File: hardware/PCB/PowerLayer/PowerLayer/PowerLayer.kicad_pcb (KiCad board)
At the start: 2 copper layers, 81.5 x 58.2 mm, 2 parts, among them J1 Conn_01x03_Female

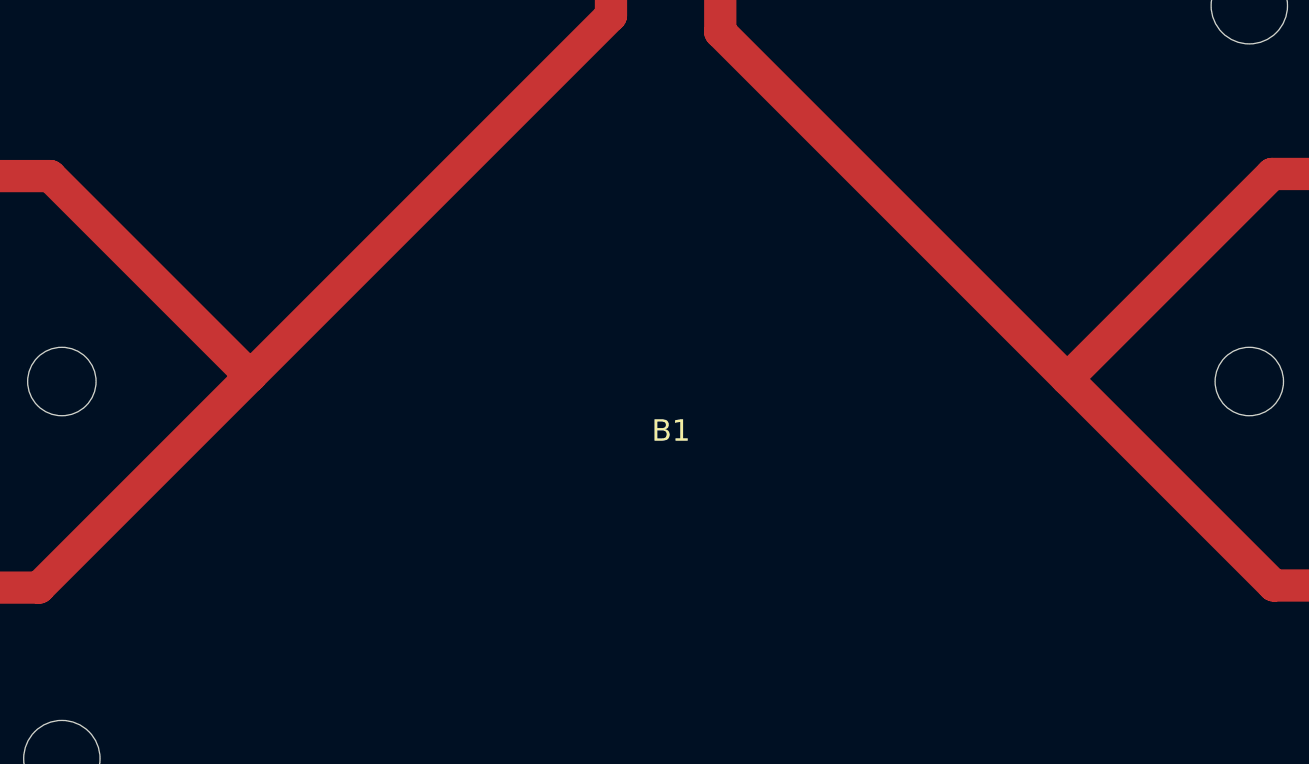
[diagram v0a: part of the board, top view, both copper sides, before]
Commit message: PowerLayer PCB batterys polarization label added
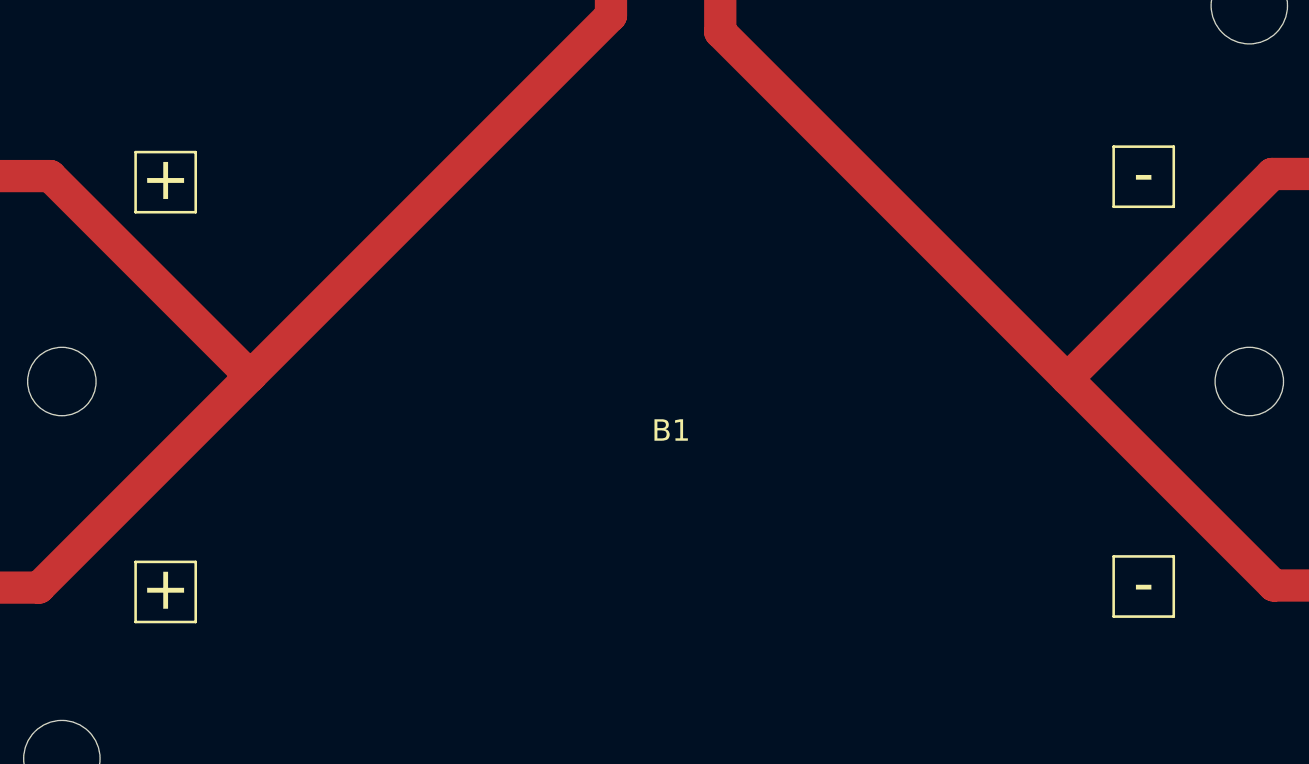
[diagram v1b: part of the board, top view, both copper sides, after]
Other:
- board text added: "+"
- board text added: "-"
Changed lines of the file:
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@@
   (general
     (thickness 1.6)
-    (drawings 14)
+    (drawings 34)
     (tracks 13)
     (zones 0)
@@
   )
   (setup
-    (last_trace_width 1.5)
+    (last_trace_width 0.25)
     (user_trace_width 1.5)
     (trace_clearance 0.2)
@@
       (effects (font (size 1 1) (thickness 0.15)))
     )
+    (fp_line (start -1.27 -1.27) (end 0.635 -1.27) (layer F.Fab) (width 0.1))
+    (fp_line (start 0.635 -1.27) (end 1.27 -0.635) (layer F.Fab) (width 0.1))
+    (fp_line (start 1.27 -0.635) (end 1.27 6.35) (layer F.Fab) (width 0.1))
+    (fp_line (start 1.27 6.35) (end -1.27 6.35) (layer F.Fab) (width 0.1))
+    (fp_line (start -1.27 6.35) (end -1.27 -1.27) (layer F.Fab) (width 0.1))
+    (fp_line (start -1.33 1.27) (end 1.33 1.27) (layer F.SilkS) (width 0.12))
+    (fp_line (start -1.33 1.27) (end -1.33 6.41) (layer F.SilkS) (width 0.12))
+    (fp_line (start -1.33 6.41) (end 1.33 6.41) (layer F.SilkS) (width 0.12))
+    (fp_line (start 1.33 1.27) (end 1.33 6.41) (layer F.SilkS) (width 0.12))
+    (fp_line (start 1.33 -1.33) (end 1.33 0) (layer F.SilkS) (width 0.12))
+    (fp_line (start 0 -1.33) (end 1.33 -1.33) (layer F.SilkS) (width 0.12))
+    (fp_line (start -1.8 -1.8) (end 1.75 -1.8) (layer F.CrtYd) (width 0.05))
+    (fp_line (start 1.75 -1.8) (end 1.75 6.85) (layer F.CrtYd) (width 0.05))
+    (fp_line (start 1.75 6.85) (end -1.8 6.85) (layer F.CrtYd) (width 0.05))
     (fp_line (start -1.8 6.85) (end -1.8 -1.8) (layer F.CrtYd) (width 0.05))
-    (fp_line (start 1.75 6.85) (end -1.8 6.85) (layer F.CrtYd) (width 0.05))
-    (fp_line (start 1.75 -1.8) (end 1.75 6.85) (layer F.CrtYd) (width 0.05))
-    (fp_line (start -1.8 -1.8) (end 1.75 -1.8) (layer F.CrtYd) (width 0.05))
-    (fp_line (start 0 -1.33) (end 1.33 -1.33) (layer F.SilkS) (width 0.12))
-    (fp_line (start 1.33 -1.33) (end 1.33 0) (layer F.SilkS) (width 0.12))
-    (fp_line (start 1.33 1.27) (end 1.33 6.41) (layer F.SilkS) (width 0.12))
-    (fp_line (start -1.33 6.41) (end 1.33 6.41) (layer F.SilkS) (width 0.12))
-    (fp_line (start -1.33 1.27) (end -1.33 6.41) (layer F.SilkS) (width 0.12))
-    (fp_line (start -1.33 1.27) (end 1.33 1.27) (layer F.SilkS) (width 0.12))
-    (fp_line (start -1.27 6.35) (end -1.27 -1.27) (layer F.Fab) (width 0.1))
-    (fp_line (start 1.27 6.35) (end -1.27 6.35) (layer F.Fab) (width 0.1))
-    (fp_line (start 1.27 -0.635) (end 1.27 6.35) (layer F.Fab) (width 0.1))
-    (fp_line (start 0.635 -1.27) (end 1.27 -0.635) (layer F.Fab) (width 0.1))
-    (fp_line (start -1.27 -1.27) (end 0.635 -1.27) (layer F.Fab) (width 0.1))
     (fp_text user %R (at 0 2.54) (layer F.Fab)
       (effects (font (size 1 1) (thickness 0.15)))
@@
       (effects (font (size 1 1) (thickness 0.15)))
     )
+    (fp_line (start -4 -39) (end 76 -39) (layer F.SilkS) (width 0.12))
+    (fp_line (start 76 4) (end 76 -39) (layer F.SilkS) (width 0.12))
+    (fp_line (start -4 4) (end -4 -39) (layer F.SilkS) (width 0.12))
     (fp_line (start -4 4) (end 76 4) (layer F.SilkS) (width 0.12))
-    (fp_line (start -4 4) (end -4 -39) (layer F.SilkS) (width 0.12))
-    (fp_line (start 76 4) (end 76 -39) (layer F.SilkS) (width 0.12))
-    (fp_line (start -4 -39) (end 76 -39) (layer F.SilkS) (width 0.12))
     (pad "" np_thru_hole circle (at 72.22 0) (size 2.38 2.38) (drill 2.38) (layers *.Cu *.Mask))
     (pad "" np_thru_hole circle (at 63.71 -35) (size 3.55 3.55) (drill 3.55) (layers *.Cu *.Mask))
@@
     )
   )
+  (gr_text + (at 82.422217 131.300546) (layer F.SilkS)
+    (effects (font (size 2 2) (thickness 0.15)))
+  )
+  (gr_text + (at 82.422217 150.350546) (layer F.SilkS)
+    (effects (font (size 2 2) (thickness 0.15)))
+  )
+  (gr_line (start 83.82 149.098) (end 83.82 151.892) (layer F.SilkS) (width 0.12))
+  (gr_line (start 83.82 151.892) (end 81.026 151.892) (layer F.SilkS) (width 0.12))
+  (gr_line (start 81.026 151.892) (end 81.026 149.098) (layer F.SilkS) (width 0.12))
+  (gr_line (start 83.82 132.842) (end 81.026 132.842) (layer F.SilkS) (width 0.12))
+  (gr_line (start 81.026 149.098) (end 83.82 149.098) (layer F.SilkS) (width 0.12))
+  (gr_line (start 81.026 132.842) (end 81.026 130.048) (layer F.SilkS) (width 0.12))
+  (gr_line (start 81.026 130.048) (end 83.82 130.048) (layer F.SilkS) (width 0.12))
+  (gr_line (start 83.82 130.048) (end 83.82 132.842) (layer F.SilkS) (width 0.12))
+  (gr_text - (at 127.888217 150.096546) (layer F.SilkS)
+    (effects (font (size 2 2) (thickness 0.15)))
+  )
+  (gr_line (start 129.286 151.638) (end 126.492 151.638) (layer F.SilkS) (width 0.12))
+  (gr_line (start 126.492 151.638) (end 126.492 148.844) (layer F.SilkS) (width 0.12))
+  (gr_line (start 126.492 148.844) (end 129.286 148.844) (layer F.SilkS) (width 0.12))
+  (gr_line (start 129.286 148.844) (end 129.286 151.638) (layer F.SilkS) (width 0.12))
+  (gr_line (start 126.492 132.588) (end 126.492 129.794) (layer F.SilkS) (width 0.12))
+  (gr_line (start 129.286 132.588) (end 126.492 132.588) (layer F.SilkS) (width 0.12))
+  (gr_line (start 129.286 129.794) (end 129.286 132.588) (layer F.SilkS) (width 0.12))
+  (gr_line (start 126.492 129.794) (end 129.286 129.794) (layer F.SilkS) (width 0.12))
+  (gr_text - (at 127.888217 131.046546) (layer F.SilkS)
+    (effects (font (size 2 2) (thickness 0.15)))
+  )
   (dimension 81.534 (width 0.15) (layer Dwgs.User)

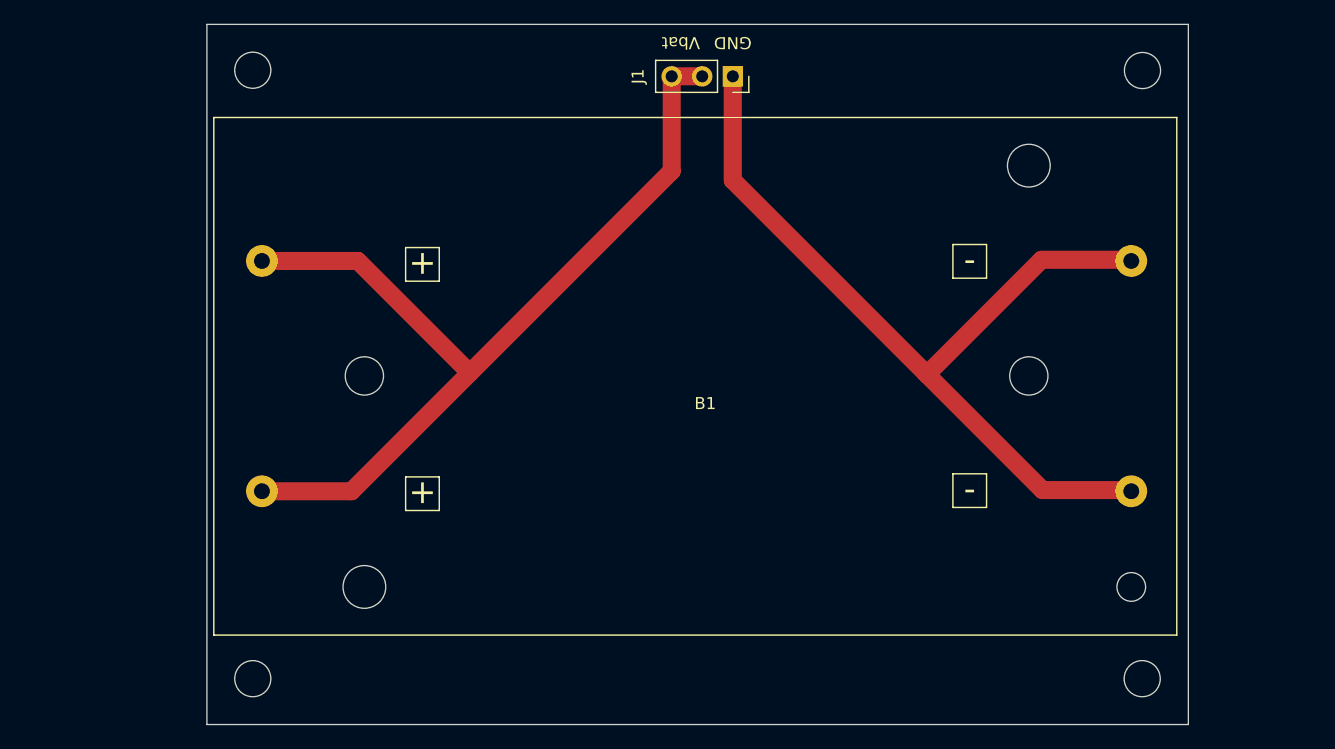
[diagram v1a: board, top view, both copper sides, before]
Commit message: Final casing selected and PCB rearranged to fit into the casing
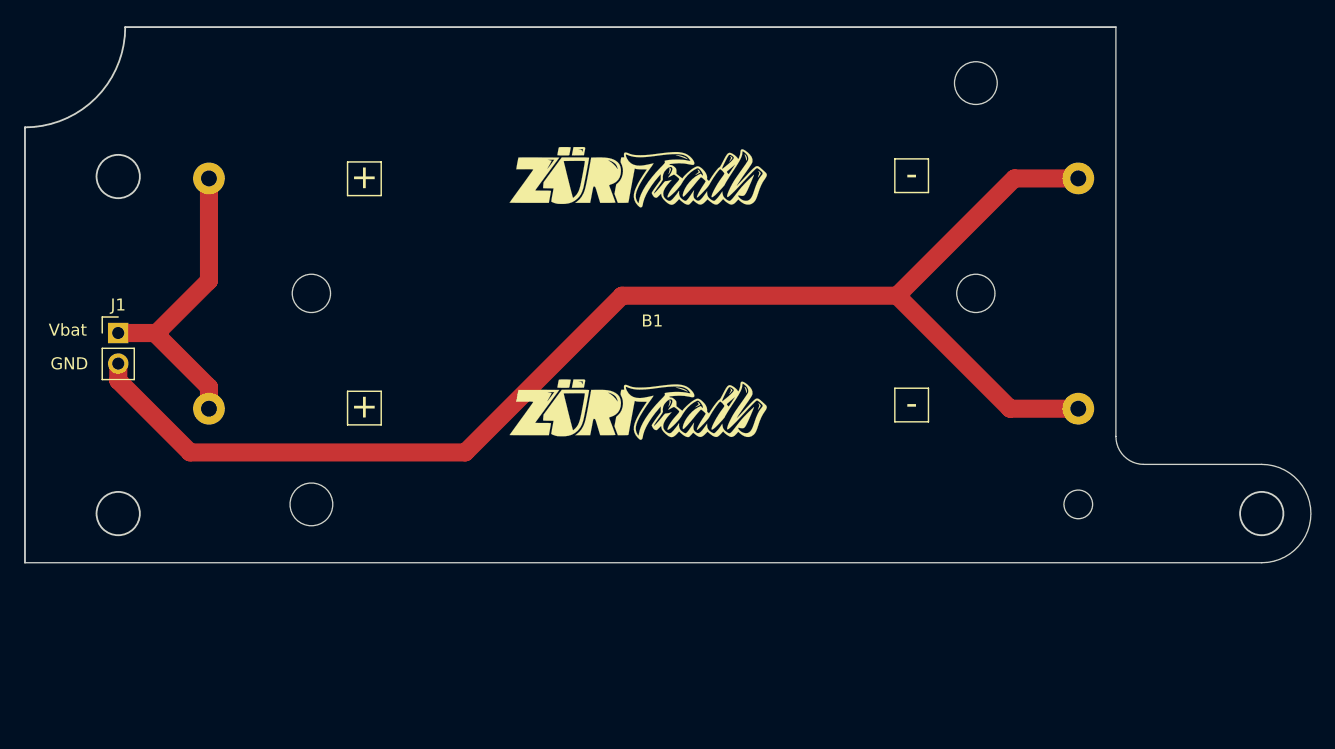
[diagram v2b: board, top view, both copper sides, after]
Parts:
- added G***: LOGO, GraphicsLib:ZueriTrailsLogo_small, F.Cu at (100.3, 124.2)
- added G***: LOGO, GraphicsLib:ZueriTrailsLogo_small, F.Cu at (100.3, 143.5)
- J1: value Conn_01x03_Female -> Logic layer connection; footprint Connector_PinSocket_2.54mm:PinSocket_1x03_P2.54mm_Vertical -> Connector_PinHeader_2.54mm:PinHeader_1x02_P2.54mm_Vertical
- moved J1 55.3 mm to (57.1, 137.1), turned to 0 degrees
- moved B1 8.15 mm to (64.7, 151.4)
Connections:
- J1 pad 1: GND -> +3V8
- J1 pad 2: +3V8 -> GND
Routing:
- net +3V8: track 76.6 -> 29.0 mm
- net GND: track 73.3 -> 112.0 mm
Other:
- board size 81.5 x 58.2 mm -> 106.8 x 44.5 mm

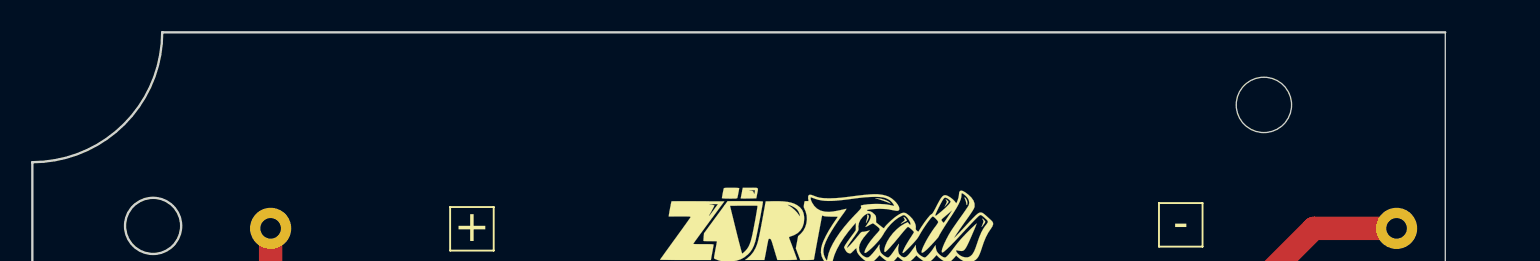
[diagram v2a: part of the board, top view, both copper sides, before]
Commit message: PCB adjusted and BOM started
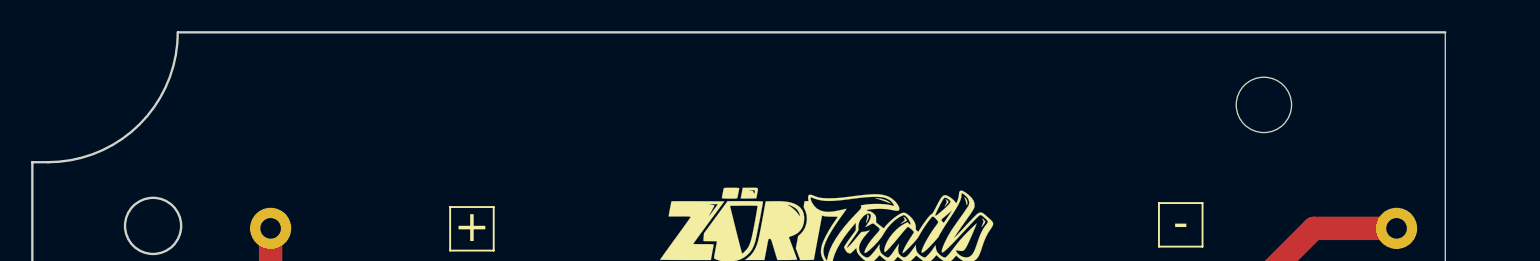
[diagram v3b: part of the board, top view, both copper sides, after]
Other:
- outline, holes or cut-outs redrawn

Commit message: BOM finished and Gerber files created
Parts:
- added REF**: MountingHole_3.5mm_Pad, MountingHole:MountingHole_3.5mm_Pad, F.Cu at (152.1, 152.1)
- added REF**: MountingHole_3.5mm_Pad, MountingHole:MountingHole_3.5mm_Pad, F.Cu at (57.1, 152.1)
- added REF**: MountingHole_3.5mm_Pad, MountingHole:MountingHole_3.5mm_Pad, F.Cu at (57.1, 124.1)
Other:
- outline, holes or cut-outs redrawn
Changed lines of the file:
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@@
   (general
     (thickness 1.6)
-    (drawings 43)
+    (drawings 39)
     (tracks 15)
     (zones 0)
-    (modules 4)
+    (modules 7)
     (nets 3)
   )
@@
     (pcbplotparams
       (layerselection 0x010fc_ffffffff)
-      (usegerberextensions false)
-      (usegerberattributes true)
-      (usegerberadvancedattributes true)
-      (creategerberjobfile true)
+      (usegerberextensions true)
+      (usegerberattributes false)
+      (usegerberadvancedattributes false)
+      (creategerberjobfile false)
       (excludeedgelayer true)
       (linewidth 0.100000)
@@
       (psa4output false)
       (plotreference true)
-      (plotvalue true)
+      (plotvalue false)
       (plotinvisibletext false)
       (padsonsilk false)
-      (subtractmaskfromsilk false)
+      (subtractmaskfromsilk true)
       (outputformat 1)
       (mirror false)
-      (drillshape 1)
+      (drillshape 0)
       (scaleselection 1)
-      (outputdirectory ""))
+      (outputdirectory "GerberFiles/v0.1/"))
   )
   (net 0 "")
@@
     (uvia_dia 0.3)
     (uvia_drill 0.1)
+  )
+  (module MountingHole:MountingHole_3.5mm_Pad (layer F.Cu)
+    (at 152.146 152.146)
+    (descr "Mounting Hole 3.5mm")
+    (tags "mounting hole 3.5mm")
+    (attr virtual)
+    (fp_text reference REF** (at 0 -4.5) (layer Dwgs.User)
+      (effects (font (size 1 1) (thickness 0.15)))
+    )
+    (fp_text value MountingHole_3.5mm_Pad (at 0 4.5) (layer F.Fab)
+      (effects (font (size 1 1) (thickness 0.15)))
+    )
+    (fp_circle (center 0 0) (end 3.5 0) (layer Cmts.User) (width 0.15))
+    (fp_circle (center 0 0) (end 3.75 0) (layer F.CrtYd) (width 0.05))
+    (fp_text user %R (at 0.3 0) (layer F.Fab)
+      (effects (font (size 1 1) (thickness 0.15)))
+    )
+    (pad 1 thru_hole circle (at 0 0) (size 7 7) (drill 3.5) (layers *.Cu *.Mask))
+  )
+  (module MountingHole:MountingHole_3.5mm_Pad (layer F.Cu)
+    (at 57.146 152.146)
+    (descr "Mounting Hole 3.5mm")
+    (tags "mounting hole 3.5mm")
+    (attr virtual)
+    (fp_text reference REF** (at 0 -4.5) (layer Dwgs.User)
+      (effects (font (size 1 1) (thickness 0.15)))
+    )
+    (fp_text value MountingHole_3.5mm_Pad (at 0 4.5) (layer F.Fab)
+      (effects (font (size 1 1) (thickness 0.15)))
+    )
+    (fp_circle (center 0 0) (end 3.5 0) (layer Cmts.User) (width 0.15))
+    (fp_circle (center 0 0) (end 3.75 0) (layer F.CrtYd) (width 0.05))
+    (fp_text user %R (at 0.3 0) (layer F.Fab)
+      (effects (font (size 1 1) (thickness 0.15)))
+    )
+    (pad 1 thru_hole circle (at 0 0) (size 7 7) (drill 3.5) (layers *.Cu *.Mask))
+  )
+  (module MountingHole:MountingHole_3.5mm_Pad (layer F.Cu)
+    (at 57.146 124.146)
+    (descr "Mounting Hole 3.5mm")
+    (tags "mounting hole 3.5mm")
+    (attr virtual)
+    (fp_text reference REF** (at 0 -4.5) (layer Dwgs.User)
+      (effects (font (size 1 1) (thickness 0.15)))
+    )
+    (fp_text value MountingHole_3.5mm_Pad (at 0 4.5) (layer F.Fab)
+      (effects (font (size 1 1) (thickness 0.15)))
+    )
+    (fp_text user %R (at 0.3 0) (layer F.Fab)
+      (effects (font (size 1 1) (thickness 0.15)))
+    )
+    (fp_circle (center 0 0) (end 3.5 0) (layer Cmts.User) (width 0.15))
+    (fp_circle (center 0 0) (end 3.75 0) (layer F.CrtYd) (width 0.05))
+    (pad 1 thru_hole circle (at 0 0) (size 7 7) (drill 3.5) (layers *.Cu *.Mask))
   )
   (module GraphicsLib:ZueriTrailsLogo_small (layer F.Cu)
@@
   (gr_arc (start 152.146 152.146) (end 152.146 156.231) (angle -180) (layer Edge.Cuts) (width 0.05))
   (gr_line (start 49.401 156.231) (end 152.146 156.231) (layer Edge.Cuts) (width 0.05))
-  (gr_circle (center 57.146 124.146) (end 60.646 124.146) (layer Dwgs.User) (width 0.15))
   (gr_circle (center 152.146 124.146) (end 150.346 124.146) (layer Dwgs.User) (width 0.15))
-  (gr_circle (center 57.146 152.146) (end 58.946 152.146) (layer Edge.Cuts) (width 0.15))
-  (gr_circle (center 57.146 124.146) (end 58.946 124.146) (layer Edge.Cuts) (width 0.15))
-  (gr_circle (center 152.146 152.146) (end 153.946 152.146) (layer Edge.Cuts) (width 0.15))
   (gr_arc (start 50.401 111.731) (end 58.731 111.731) (angle 90) (layer Edge.Cuts) (width 0.15))
   (gr_line (start 60.931 156.231) (end 49.401 156.231) (layer Dwgs.User) (width 0.15))
